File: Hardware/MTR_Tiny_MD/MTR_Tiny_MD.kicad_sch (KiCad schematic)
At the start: 81 parts, among them J1 USB_C_Receptacle_USB2.0, J2 68021-412HLF, J3 LED OUT, J4 UART, J5 LED OUT, J6 XT30PB, Q1 AO3401A, SW1 Boot, SW2 Reset, U1 RP2040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

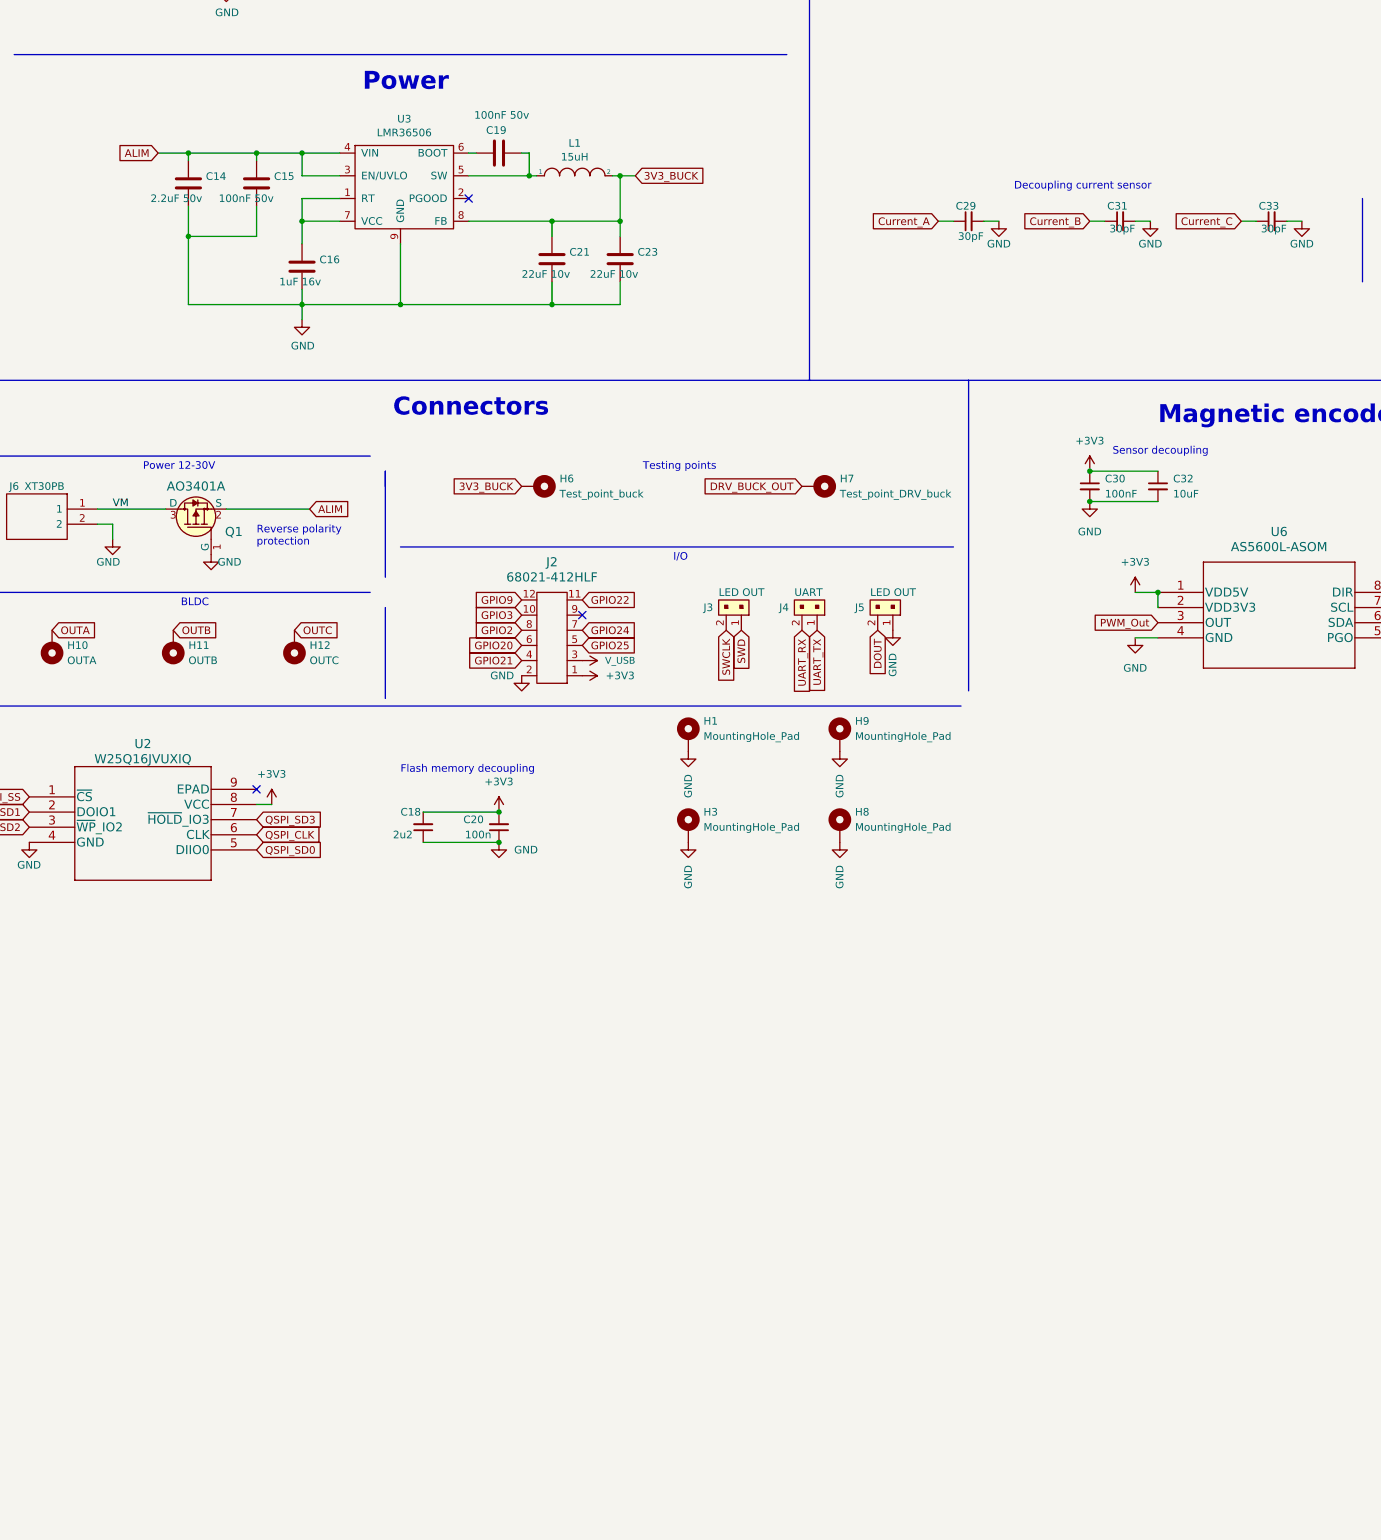
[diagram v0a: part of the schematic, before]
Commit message: new DCDC convert
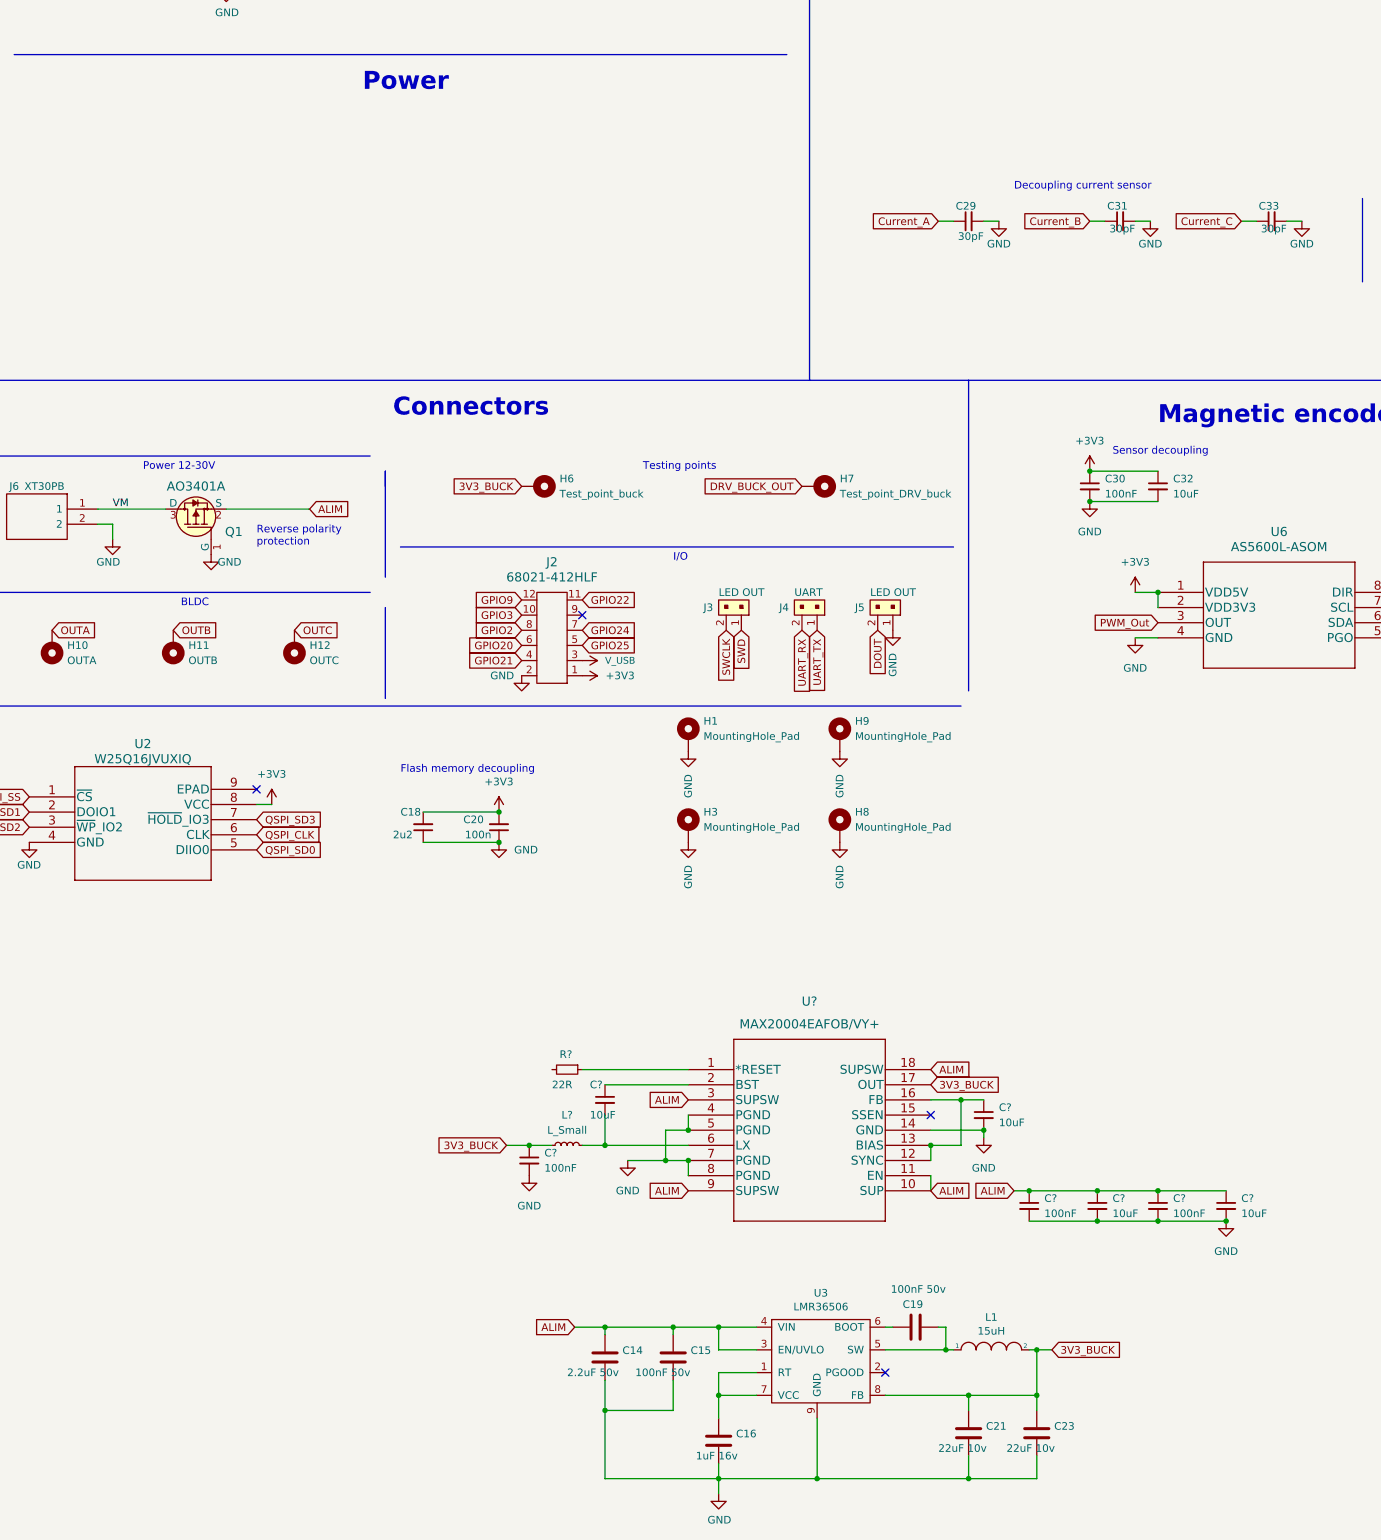
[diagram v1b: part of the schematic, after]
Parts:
- added C? (x3): 100nF, Capacitor_SMD:C_0402_1005Metric, symbol Device:C_Small
- added C? (x4): 10uF, Capacitor_SMD:C_0402_1005Metric, symbol Device:C_Small
- added L?: L_Small, symbol Device:L_Small
- added R?: 22R, Resistor_SMD:R_0603_1608Metric, symbol Device:R_Small
- added U?: MAX20004EAFOB/VY+, Personal:MAX20004EAFOB&slash_VY&plus_, symbol 2023-02-26_00-40-49:MAX20004EAFOB/VY+
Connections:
- net +3V3: now also C?.1, L?.1, U?.17 (OUT)
- net ALIM: now also C?.1, C?.1, C?.1, C?.1, U?.10 (SUP), U?.11 (EN), U?.18 (SUPSW), U?.3 (SUPSW), U?.9 (SUPSW)
- net GND: now also C?.2, C?.2, C?.2, C?.2, C?.2, C?.2, U?.14 (GND), U?.4 (PGND), U?.5 (PGND), U?.7 (PGND), U?.8 (PGND)
- new net: C?.1, U?.12 (SYNC), U?.13 (BIAS), U?.16 (FB)
- new net: C?.1, U?.2 (BST)
- new net: C?.2, L?.2, U?.6 (LX)
- new net: R?.1, U?.1 (*RESET)
- no-connect marks 11 -> 12
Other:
- moved on the sheet: C14, C15, C16, C19, C21, C23, L1, U3

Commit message: Add new Vbuck
LMR36506 to MAX15462AATA+T
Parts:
- removed C14: 2.2uF 50v, Capacitor_SMD:C_0805_2012Metric, symbol Device:C
- removed C15, C19: 100nF 50v, Capacitor_SMD:C_0603_1608Metric, symbol Device:C
- removed C16: 1uF 16v, Capacitor_SMD:C_0603_1608Metric, symbol Device:C
- removed C21, C23: 22uF 10v, Capacitor_SMD:C_0603_1608Metric, symbol Device:C
- removed C? (x3): 100nF, Capacitor_SMD:C_0402_1005Metric, symbol Device:C_Small
- removed C? (x4): 10uF, Capacitor_SMD:C_0402_1005Metric, symbol Device:C_Small
- removed L1: 15uH, Inductor_SMD:L_1210_3225Metric, symbol pspice:INDUCTOR
- removed L?: L_Small, symbol Device:L_Small
- removed R?: 22R, Resistor_SMD:R_0603_1608Metric, symbol Device:R_Small
- removed U3: LMR36506, Personal:LMR36506, symbol DriverParts:LMR36506
- removed U?: MAX20004EAFOB/VY+, Personal:MAX20004EAFOB&slash_VY&plus_, symbol 2023-02-26_00-40-49:MAX20004EAFOB/VY+
- added C38, C39: 1uF 50V, Capacitor_SMD:C_1206_3216Metric, symbol Device:C_Small
- added C40: 10uF 10V, Capacitor_SMD:C_1206_3216Metric, symbol Device:C_Small
- added C41, C42: 22uF 10v, Capacitor_SMD:C_0603_1608Metric, symbol Device:C
- added F1: 500mA, Fuse:Fuse_0603_1608Metric, symbol Device:Fuse_Small
- added F2: 250mA, Fuse:Fuse_0603_1608Metric, symbol Device:Fuse_Small
- added L2: 33uH, Inductor_SMD:L_1210_3225Metric, symbol Device:L_Small
- added U7: MAX15462AATA+T, footprints:21-0487_T822CN&plus_1_MXM, symbol 2023-04-22_15-23-11:MAX15462AATA+T
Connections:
- net +3V3: now also F2.2
- net ALIM: now also C38.1, U7.1 (VIN), U7.2 (EN/UVLO)
- net GND: now also C38.2, C39.2, C40.2, C41.2, C42.2, U7.5 (MODE), U7.6 (*RESET), U7.7 (GND)
- net V_USB: now also F1.1; no longer U4.2 (IN), U4.6 (EN1)
- new net: L2.1, U7.8 (LX)
- new net: F1.2, U4.2 (IN), U4.6 (EN1)
- new net: C39.1, U7.3 (VCC)
- new net FeedBack: C40.1, C41.1, C42.1, F2.1, L2.2, U7.4 (FB/VOUT)
- no-connect marks 12 -> 10

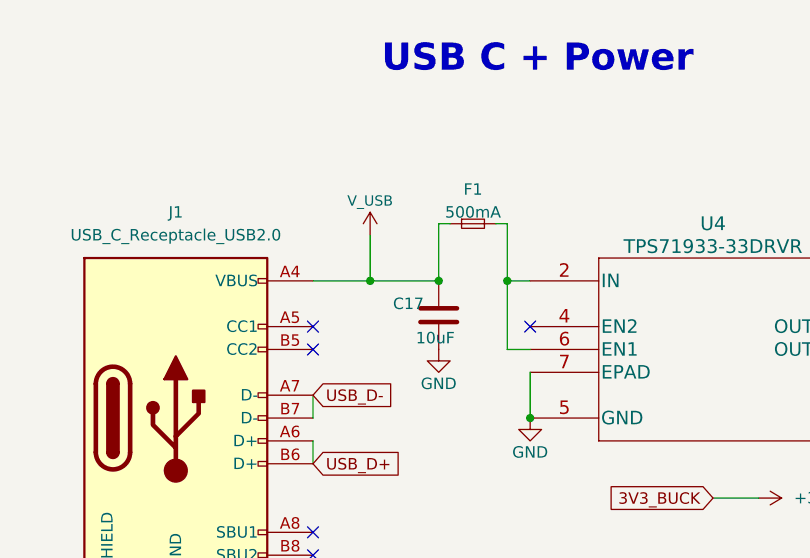
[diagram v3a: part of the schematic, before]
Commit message: Silkscreen labelling - RFP
Ready For Production Rev 1.1
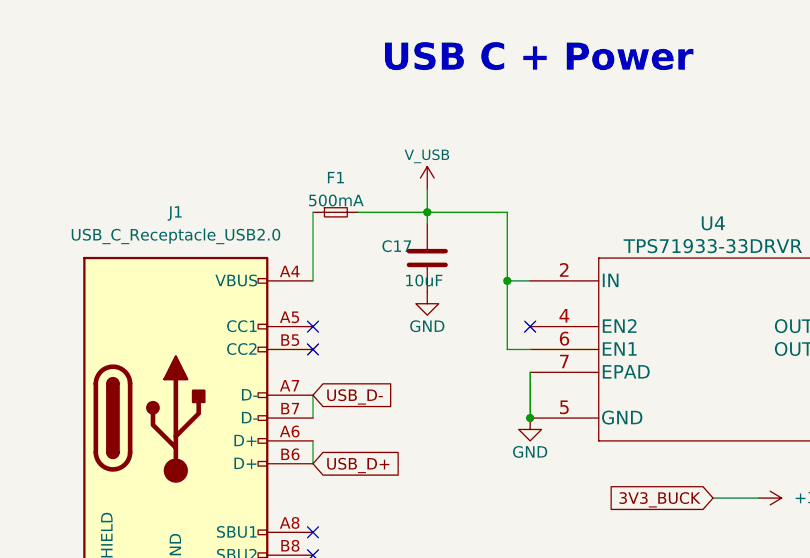
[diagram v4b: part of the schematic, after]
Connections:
- net V_USB: now also F1.2, U4.2 (IN), U4.6 (EN1); no longer F1.1, J1.A4 (VBUS), J1.A9 (VBUS), J1.B4 (VBUS), J1.B9 (VBUS)
- new net: F1.1, J1.A4 (VBUS), J1.A9 (VBUS), J1.B4 (VBUS), J1.B9 (VBUS)
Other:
- moved on the sheet: C17, F1
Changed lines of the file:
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@@
   (title_block
     (title "MTR Tiny MD")
-    (rev "V1")
+    (rev "V1.1")
     (company "More Than Robots")
     (comment 1 "Ciciliano ALTMANN")
@@
   (junction (at 288.29 92.71) (diameter 0) (color 0 0 0 0)
   )
-  (junction (at 193.04 41.91) (diameter 0) (color 0 0 0 0)
-  )
   (junction (at 25.4 63.5) (diameter 0) (color 0 0 0 0)
   )
@@
   (junction (at 227.33 184.15) (diameter 0) (color 0 0 0 0)
   )
-  (junction (at 185.42 41.91) (diameter 0) (color 0 0 0 0)
-  )
   (junction (at 295.91 110.49) (diameter 0) (color 0 0 0 0)
   )
   (junction (at 382.27 67.31) (diameter 0) (color 0 0 0 0)
   )
+  (junction (at 191.77 34.29) (diameter 0) (color 0 0 0 0)
+  )
   (junction (at 320.04 213.36) (diameter 0) (color 0 0 0 0)
   )
@@
     (stroke (width 0) (type default))
   )
-  (wire (pts (xy 185.42 36.83) (xy 185.42 41.91))
-    (stroke (width 0) (type default))
-  )
-  (wire (pts (xy 199.39 35.56) (xy 200.66 35.56))
-    (stroke (width 0) (type default))
-  )
   (wire (pts (xy 393.7 173.99) (xy 391.16 173.99))
     (stroke (width 0) (type default))
   )
-  (wire (pts (xy 194.31 35.56) (xy 193.04 35.56))
-    (stroke (width 0) (type default))
-  )
-  (wire (pts (xy 185.42 41.91) (xy 193.04 41.91))
-    (stroke (width 0) (type default))
-  )
   (wire (pts (xy 307.34 95.25) (xy 295.91 95.25))
     (stroke (width 0) (type default))
@@
     (stroke (width 0) (type default))
   )
-  (wire (pts (xy 193.04 35.56) (xy 193.04 41.91))
-    (stroke (width 0) (type default))
-  )
   (wire (pts (xy 284.48 87.63) (xy 288.29 87.63))
     (stroke (width 0) (type default))
@@
     (stroke (width 0) (type default))
   )
-  (wire (pts (xy 200.66 35.56) (xy 200.66 41.91))
+  (wire (pts (xy 191.77 34.29) (xy 191.77 35.56))
+    (stroke (width 0) (type default))
+  )
+  (wire (pts (xy 200.66 34.29) (xy 200.66 41.91))
     (stroke (width 0) (type default))
   )
@@
     (stroke (width 0) (type default))
   )
+  (wire (pts (xy 191.77 34.29) (xy 200.66 34.29))
+    (stroke (width 0) (type default))
+  )
   (wire (pts (xy 382.27 74.93) (xy 382.27 77.47))
     (stroke (width 0) (type default))
@@
     (stroke (width 0) (type default))
   )
+  (wire (pts (xy 179.07 34.29) (xy 179.07 41.91))
+    (stroke (width 0) (type default))
+  )
   (wire (pts (xy 45.72 54.61) (xy 54.61 54.61))
     (stroke (width 0) (type default))
@@
     (stroke (width 0) (type default))
   )
+  (wire (pts (xy 191.77 31.75) (xy 191.77 34.29))
+    (stroke (width 0) (type default))
+  )
   (wire (pts (xy 189.23 173.99) (xy 189.23 184.15))
     (stroke (width 0) (type default))
@@
     (stroke (width 0) (type default))
   )
-  (wire (pts (xy 179.07 41.91) (xy 185.42 41.91))
-    (stroke (width 0) (type default))
-  )
   (wire (pts (xy 67.31 59.69) (xy 67.31 66.04))
     (stroke (width 0) (type default))
@@
     (stroke (width 0) (type default))
   )
+  (wire (pts (xy 184.15 34.29) (xy 191.77 34.29))
+    (stroke (width 0) (type default))
+  )
   (wire (pts (xy 248.92 124.46) (xy 251.46 124.46))
     (stroke (width 0) (type default))
@@
     )
   )
-  (symbol (lib_id "SparkFun-PowerSymbols:V_USB") (at 185.42 36.83 0) (unit 1)
+  (symbol (lib_id "SparkFun-PowerSymbols:V_USB") (at 191.77 31.75 0) (unit 1)
     (in_bom yes) (on_board yes) (dnp no)
-    (property "Reference" "#SUPPLY0102" (at 186.69 36.83 0)
+    (property "Reference" "#SUPPLY0102" (at 193.04 31.75 0)
       (effects (font (size 1.143 1.143)) (justify left bottom) hide)
     )
-    (property "Value" "V_USB" (at 185.42 33.02 0)
+    (property "Value" "V_USB" (at 191.77 27.94 0)
       (effects (font (size 1.143 1.143)))
     )
-    (property "Footprint" "XXX-00000" (at 185.42 33.02 0)
+    (property "Footprint" "XXX-00000" (at 191.77 27.94 0)
       (effects (font (size 1.524 1.524)) hide)
     )
-    (property "Datasheet" "" (at 185.42 36.83 0)
+    (property "Datasheet" "" (at 191.77 31.75 0)
       (effects (font (size 1.524 1.524)) hide)
     )
@@
     )
   )
-  (symbol (lib_id "Device:Fuse_Small") (at 196.85 35.56 0) (unit 1)
+  (symbol (lib_id "Device:Fuse_Small") (at 181.61 34.29 0) (unit 1)
     (in_bom yes) (on_board yes) (dnp no) (fields_autoplaced)
-    (property "Reference" "F1" (at 196.85 31.75 0)
+    (property "Reference" "F1" (at 181.61 30.48 0)
       (effects (font (size 1.27 1.27)))
     )
-    (property "Value" "500mA" (at 196.85 34.29 0)
+    (property "Value" "500mA" (at 181.61 33.02 0)
       (effects (font (size 1.27 1.27)))
     )
-    (property "Footprint" "Fuse:Fuse_0603_1608Metric" (at 196.85 35.56 0)
+    (property "Footprint" "Fuse:Fuse_0603_1608Metric" (at 181.61 34.29 0)
       (effects (font (size 1.27 1.27)) hide)
     )
-    (property "Datasheet" "~" (at 196.85 35.56 0)
+    (property "Datasheet" "~" (at 181.61 34.29 0)
       (effects (font (size 1.27 1.27)) hide)
     )
@@
     )
   )
-  (symbol (lib_id "power:GND") (at 193.04 49.53 0) (unit 1)
+  (symbol (lib_id "power:GND") (at 191.77 43.18 0) (unit 1)
     (in_bom yes) (on_board yes) (dnp no)
-    (property "Reference" "#PWR0128" (at 193.04 55.88 0)
+    (property "Reference" "#PWR0128" (at 191.77 49.53 0)
       (effects (font (size 1.27 1.27)) hide)
     )
-    (property "Value" "GND" (at 193.04 53.34 0)
+    (property "Value" "GND" (at 191.77 46.99 0)
       (effects (font (size 1.27 1.27)))
     )
-    (property "Footprint" "" (at 193.04 49.53 0)
+    (property "Footprint" "" (at 191.77 43.18 0)
       (effects (font (size 1.27 1.27)) hide)
     )
-    (property "Datasheet" "" (at 193.04 49.53 0)
+    (property "Datasheet" "" (at 191.77 43.18 0)
       (effects (font (size 1.27 1.27)) hide)
     )
@@
     )
   )
-  (symbol (lib_id "Device:C") (at 193.04 45.72 0) (unit 1)
+  (symbol (lib_id "Device:C") (at 191.77 39.37 0) (unit 1)
     (in_bom yes) (on_board yes) (dnp no)
-    (property "Reference" "C17" (at 187.96 44.45 0)
+    (property "Reference" "C17" (at 186.69 38.1 0)
       (effects (font (size 1.27 1.27)) (justify left))
     )
-    (property "Value" "10uF" (at 190.5 48.26 0)
+    (property "Value" "10uF" (at 189.23 41.91 0)
       (effects (font (size 1.27 1.27)) (justify left))
     )
-    (property "Footprint" "Capacitor_SMD:C_0603_1608Metric" (at 194.0052 49.53 0)
+    (property "Footprint" "Capacitor_SMD:C_0603_1608Metric" (at 192.7352 43.18 0)
       (effects (font (size 1.27 1.27)) hide)
     )
-    (property "Datasheet" "~" (at 193.04 45.72 0)
+    (property "Datasheet" "~" (at 191.77 39.37 0)
       (effects (font (size 1.27 1.27)) hide)
     )
